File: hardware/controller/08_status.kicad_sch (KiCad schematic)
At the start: 3 parts, among them U60 SN74LVC2G17DCKR

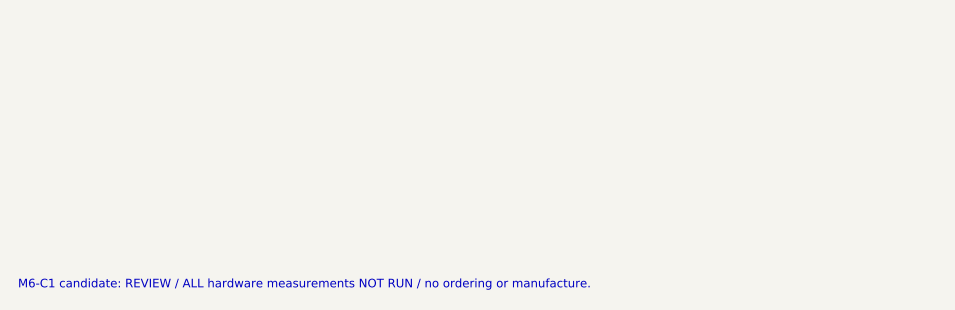
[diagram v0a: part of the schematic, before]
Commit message: M6-C1R1: protect pack identity input and review USB ESD topology
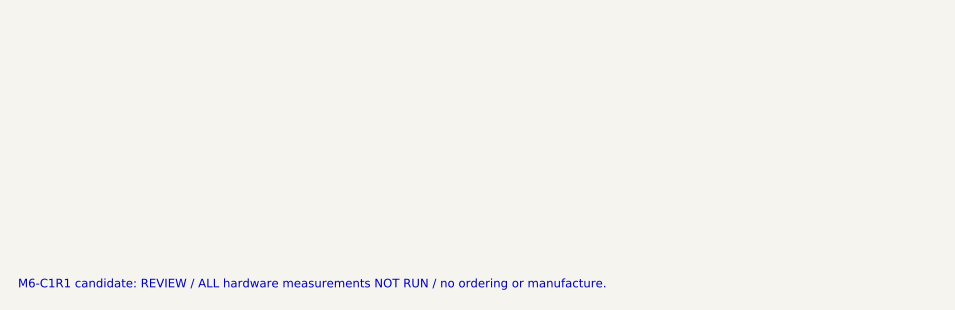
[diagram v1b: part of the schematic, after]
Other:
- note added: "M6-C1R1 candidate: REVIEW / ALL hardware measurements NOT RUN / no ordering or manufacture."
- note removed: "M6-C1 candidate: REVIEW / ALL hardware measurements NOT RUN / no ordering or manufacture."
